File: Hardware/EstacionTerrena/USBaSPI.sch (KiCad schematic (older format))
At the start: 17 parts, among them J2 USB_B_Micro, U1 TPD2E2U06, U2 MIC5323-3.3YD5_TR, U3 MCP2210, Y1 12MHz

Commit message: Corrección de librerías en PCB de estación terrena
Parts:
- removed U2: MIC5323-3.3YD5_TR, SamacSys_Parts:SOT95P280X100-5N, symbol EstacionTerrena-rescue:MIC5323-3.3YD5_TR-SamacSys_Parts
- removed U3: MCP2210, Package_SO:SSOP-20_5.3x7.2mm_P0.65mm, symbol EstacionTerrena-rescue:MCP2210-AXTEC_IC
- added U2: MIC5323-3.3YD5_TR, SOT95P280X100-5N, symbol SamacSys_Parts:MIC5323-3.3YD5_TR
- added U3: MCP2210, symbol AXTEC_IC:MCP2210
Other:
- moved on the sheet: C4
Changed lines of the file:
@@
 EESchema Schematic File Version 4
 LIBS:EstacionTerrena-cache
-EELAYER 26 0
+EELAYER 29 0
 EELAYER END
 $Descr A4 11693 8268
@@
 Wire Wire Line
 	1100 4600 1150 4600
-$Comp
-L EstacionTerrena-rescue:MCP2210-AXTEC_IC U3
-U 1 1 5B9999E2
-P 8250 4450
-F 0 "U3" H 8250 5115 50  0000 C CNN
-F 1 "MCP2210" H 8250 5024 50  0000 C CNN
-F 2 "Package_SO:SSOP-20_5.3x7.2mm_P0.65mm" H 8050 4550 50  0001 C CNN
-F 3 "http://ww1.microchip.com/downloads/en/devicedoc/22288a.pdf" H 8050 4550 50  0001 C CNN
-F 4 "MCP2210-I/SS" H 8250 4450 50  0001 C CNN "Manufacturer Part Number"
-	1    8250 4450
-	1    0    0    -1
-$EndComp
 Text Label 1650 4150 0    50   ~ 0
 D+
@@
 L power:GND #PWR018
 U 1 1 5B9A09D3
-P 8300 3500
-F 0 "#PWR018" H 8300 3250 50  0001 C CNN
-F 1 "GND" H 8305 3327 50  0000 C CNN
-F 2 "" H 8300 3500 50  0001 C CNN
-F 3 "" H 8300 3500 50  0001 C CNN
-	1    8300 3500
+P 8250 3450
+F 0 "#PWR018" H 8250 3200 50  0001 C CNN
+F 1 "GND" H 8255 3277 50  0000 C CNN
+F 2 "" H 8250 3450 50  0001 C CNN
+F 3 "" H 8250 3450 50  0001 C CNN
+	1    8250 3450
 	1    0    0    -1
 $EndComp
@@
 L power:+3V3 #PWR017
 U 1 1 5B9A0A7A
-P 8300 3200
-F 0 "#PWR017" H 8300 3050 50  0001 C CNN
-F 1 "+3V3" H 8315 3373 50  0000 C CNN
-F 2 "" H 8300 3200 50  0001 C CNN
-F 3 "" H 8300 3200 50  0001 C CNN
-	1    8300 3200
-	1    0    0    -1
-$EndComp
-Wire Wire Line
-	8300 3250 8300 3200
-Wire Wire Line
-	8300 3450 8300 3500
+P 8250 3150
+F 0 "#PWR017" H 8250 3000 50  0001 C CNN
+F 1 "+3V3" H 8265 3323 50  0000 C CNN
+F 2 "" H 8250 3150 50  0001 C CNN
+F 3 "" H 8250 3150 50  0001 C CNN
+	1    8250 3150
+	1    0    0    -1
+$EndComp
+Wire Wire Line
+	8250 3200 8250 3150
+Wire Wire Line
+	8250 3400 8250 3450
 Wire Wire Line
 	5650 4350 5650 4300
@@
 Wire Wire Line
 	4950 3950 5650 3950
-$Comp
-L EstacionTerrena-rescue:MIC5323-3.3YD5_TR-SamacSys_Parts U2
-U 1 1 5BEF597E
-P 4550 4000
-F 0 "U2" H 4550 4317 50  0000 C CNN
-F 1 "MIC5323-3.3YD5_TR" H 4550 4225 50  0000 C CNN
-F 2 "SamacSys_Parts:SOT95P280X100-5N" H 5500 4100 50  0001 L CNN
-F 3 "http://ww1.microchip.com/downloads/en/DeviceDoc/MIC5323.pdf" H 5500 4000 50  0001 L CNN
-F 4 "Micrel MIC5323-3.3YD5 TR, LDO Voltage Regulator, 300mA, 3.3 V 2%, 2.65  5.5 Vin, 5-Pin TSOT-23" H 5500 3900 50  0001 L CNN "Description"
-F 5 "1" H 5500 3800 50  0001 L CNN "Height"
-F 6 "Micrel" H 5500 3700 50  0001 L CNN "Manufacturer_Name"
-F 7 "MIC5323-3.3YD5 TR" H 5500 3600 50  0001 L CNN "Manufacturer Part Number"
-F 8 "8855996P" H 5500 3500 50  0001 L CNN "RS Part Number"
-F 9 "http://uk.rs-online.com/web/p/products/8855996P" H 5500 3400 50  0001 L CNN "RS Price/Stock"
-F 10 "MIC5323-3.3YD5 TR" H 5500 3300 50  0001 L CNN "Arrow Part Number"
-F 11 "http://uk.rs-online.com/web/p/products/8855996P" H 5500 3200 50  0001 L CNN "Arrow Price/Stock"
-	1    4550 4000
-	1    0    0    -1
-$EndComp
 $Comp
 L Device:R R2
@@
 L Device:C_Small C4
 U 1 1 5BEF7387
-P 8300 3350
-F 0 "C4" H 8392 3396 50  0000 L CNN
-F 1 "100nF" H 8392 3305 50  0000 L CNN
-F 2 "Capacitor_SMD:C_0603_1608Metric" H 8300 3350 50  0001 C CNN
-F 3 "~" H 8300 3350 50  0001 C CNN
-F 4 "X7R" H 8300 3350 50  0001 C CNN "Dielectric"
-F 5 "16V" H 8300 3350 50  0001 C CNN "Voltage"
-F 6 "EMK107B7104KAHT" H 8300 3350 50  0001 C CNN "Manufacturer Part Number"
-	1    8300 3350
+P 8250 3300
+F 0 "C4" H 8342 3346 50  0000 L CNN
+F 1 "100nF" H 8342 3255 50  0000 L CNN
+F 2 "Capacitor_SMD:C_0603_1608Metric" H 8250 3300 50  0001 C CNN
+F 3 "~" H 8250 3300 50  0001 C CNN
+F 4 "X7R" H 8250 3300 50  0001 C CNN "Dielectric"
+F 5 "16V" H 8250 3300 50  0001 C CNN "Voltage"
+F 6 "EMK107B7104KAHT" H 8250 3300 50  0001 C CNN "Manufacturer Part Number"
+	1    8250 3300
 	1    0    0    -1
 $EndComp
@@
 EndData
 $EndBitmap
+$Comp
+L SamacSys_Parts:MIC5323-3.3YD5_TR U2
+U 1 1 5CCFA0D3
+P 4550 4000
+F 0 "U2" H 4550 4315 50  0000 C CNN
+F 1 "MIC5323-3.3YD5_TR" H 4550 4224 50  0000 C CNN
+F 2 "SOT95P280X100-5N" H 5500 4100 50  0001 L CNN
+F 3 "http://ww1.microchip.com/downloads/en/DeviceDoc/MIC5323.pdf" H 5500 4000 50  0001 L CNN
+F 4 "Micrel MIC5323-3.3YD5 TR, LDO Voltage Regulator, 300mA, 3.3 V 2%, 2.65  5.5 Vin, 5-Pin TSOT-23" H 5500 3900 50  0001 L CNN "Description"
+F 5 "1" H 5500 3800 50  0001 L CNN "Height"
+F 6 "Micrel" H 5500 3700 50  0001 L CNN "Manufacturer_Name"
+F 7 "MIC5323-3.3YD5 TR" H 5500 3600 50  0001 L CNN "Manufacturer Part Number"
+F 8 "8855996P" H 5500 3500 50  0001 L CNN "RS Part Number"
+F 9 "http://uk.rs-online.com/web/p/products/8855996P" H 5500 3400 50  0001 L CNN "RS Price/Stock"
+F 10 "MIC5323-3.3YD5 TR" H 5500 3300 50  0001 L CNN "Arrow Part Number"
+F 11 "http://uk.rs-online.com/web/p/products/8855996P" H 5500 3200 50  0001 L CNN "Arrow Price/Stock"
+	1    4550 4000
+	1    0    0    -1
+$EndComp
+$Comp
+L AXTEC_IC:MCP2210 U3
+U 1 1 5CCFD092
+P 8250 4450
+F 0 "U3" H 8250 5115 50  0000 C CNN
+F 1 "MCP2210" H 8250 5024 50  0000 C CNN
+F 2 "" H 8050 4550 50  0001 C CNN
+F 3 "http://ww1.microchip.com/downloads/en/DeviceDoc/22288A.pdf" H 8050 4550 50  0001 C CNN
+F 4 "MCP2210-I/SS" H 8250 4450 50  0001 C CNN "Manufacturer Part Number"
+	1    8250 4450
+	1    0    0    -1
+$EndComp
 $EndSCHEMATC

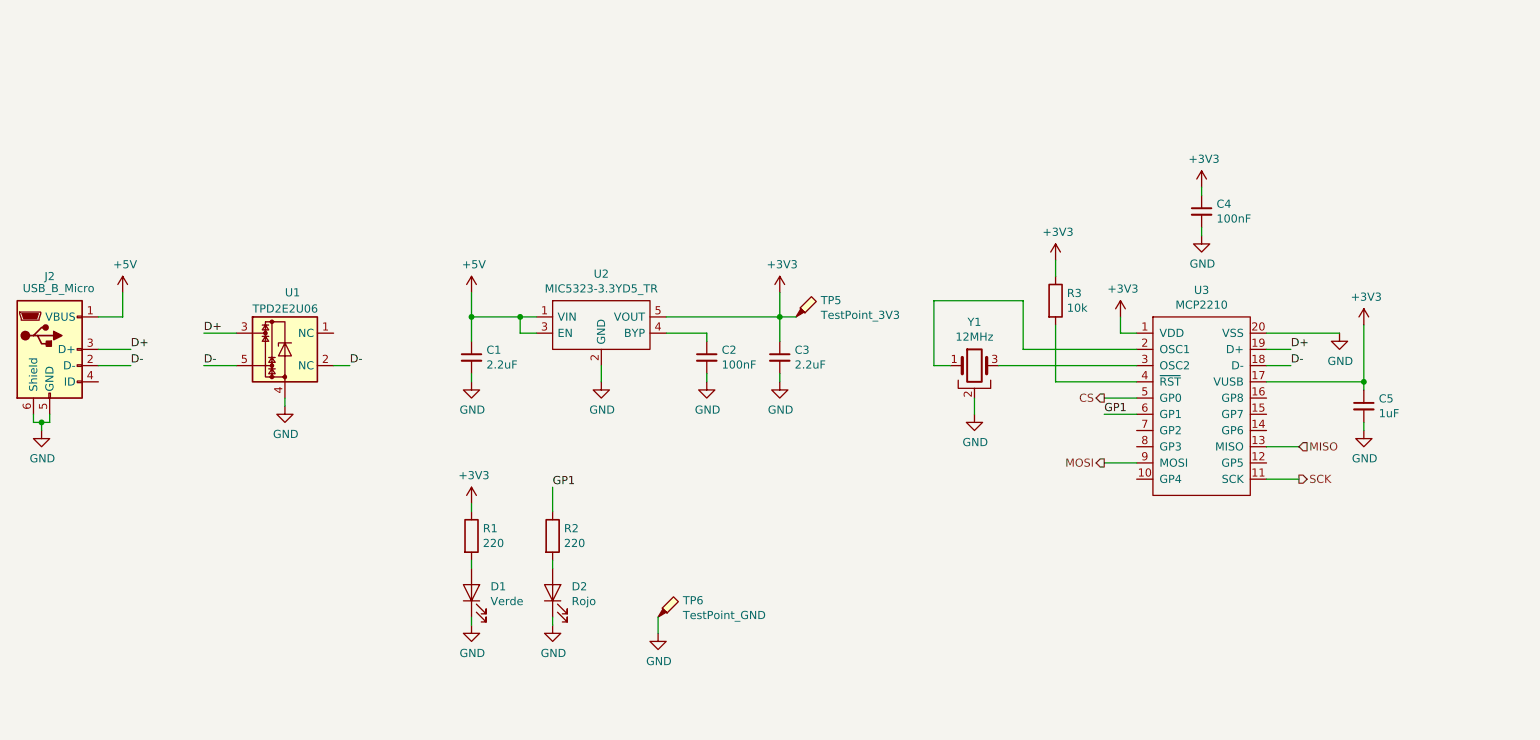
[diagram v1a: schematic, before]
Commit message: Estacion terrena:
- Nuevo LDO de 500mA para poder utilizar el CC1190 a toda su potencia de ser necesario
- Cambiado el MCP2210 por un PIC18F14K50 ya que el MCP2210 es MUY lento para transferencias SPI
- Agregado de footprints faltantes
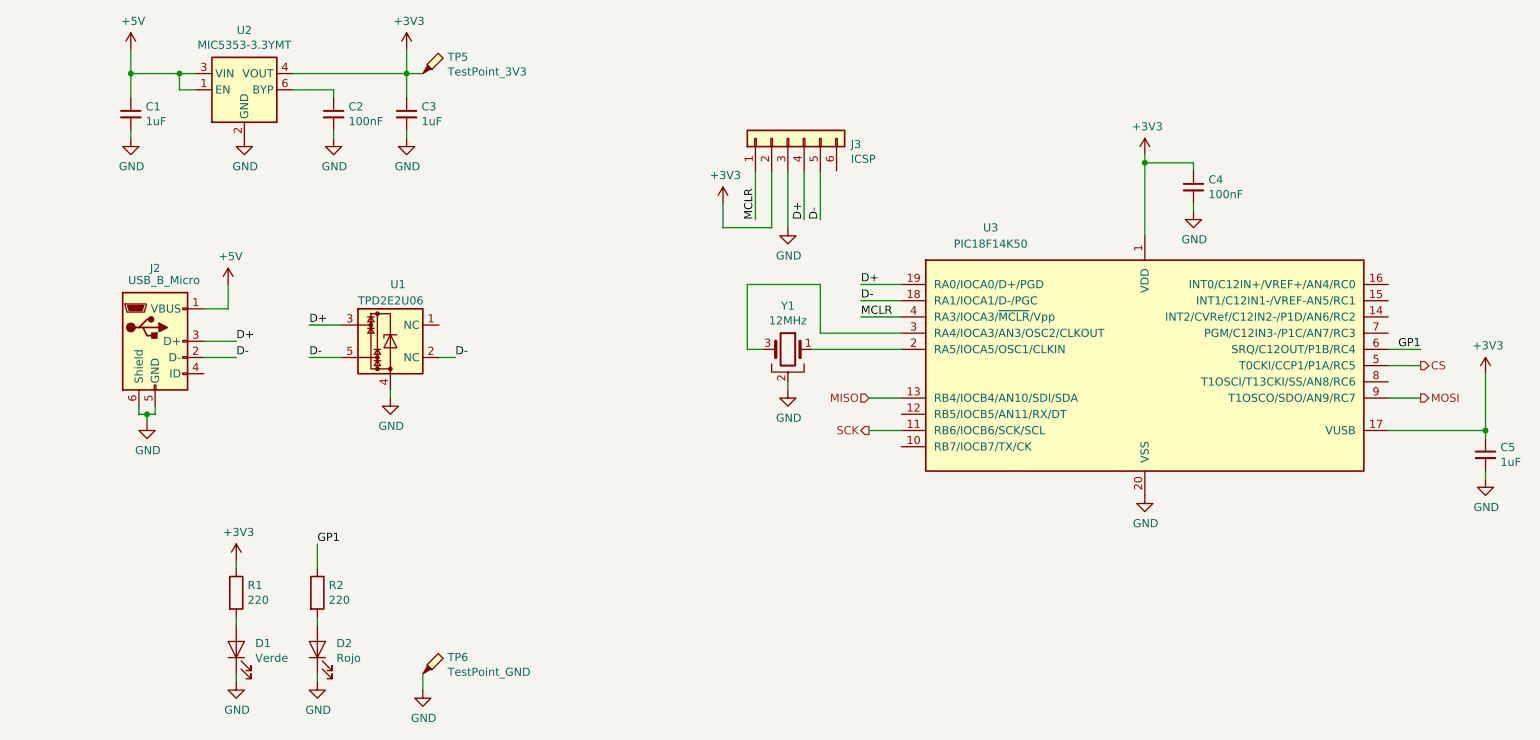
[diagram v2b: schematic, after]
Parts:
- removed R3: 10k, Resistor_SMD:R_0603_1608Metric_Pad1.05x0.95mm_HandSolder, symbol Device:R
- removed U2: MIC5323-3.3YD5_TR, SOT95P280X100-5N, symbol SamacSys_Parts:MIC5323-3.3YD5_TR
- removed U3: MCP2210, symbol AXTEC_IC:MCP2210
- added J3: ICSP, Connector_PinHeader_2.54mm:PinHeader_1x06_P2.54mm_Vertical, symbol Connector_Generic:Conn_01x06
- added U2: MIC5353-3.3YMT, Package_DFN_QFN:MLF-6-1EP_1.6x1.6mm_P0.5mm_EP0.5x1.26mm, symbol Regulator_Linear:MIC5353-3.3YMT
- added U3: PIC18F14K50, Package_SO:SSOP-20_5.3x7.2mm_P0.65mm, symbol MCU_Microchip_PIC18:PIC18F14K50-ESS
- C1, C3: value 2.2uF -> 1uF; footprint Capacitor_SMD:C_0805_2012Metric -> Capacitor_SMD:C_0603_1608Metric; Manufacturer Part Number LMK212B7225KG-T -> LMK107B7105MA-T
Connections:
- net +3V3: now also J3.2 (Pin_2), U2.4 (VOUT), U3.1 (VDD), U3.17 (VUSB)
- net +5V: now also U2.1 (EN), U2.3 (VIN)
- net CS: now also U3.5 (T0CKI/CCP1/P1A/RC5)
- net D+: now also J3.4 (Pin_4), U3.19 (RA0/IOCA0/D+/PGD)
- net D-: now also J3.5 (Pin_5), U3.18 (RA1/IOCA1/D-/PGC)
- net GND: now also J3.3 (Pin_3), U2.2 (GND), U2.7 (GND), U3.20 (VSS)
- net GP1: now also U3.6 (SRQ/C12OUT/P1B/RC4)
- net MISO: now also U3.13 (RB4/IOCB4/AN10/SDI/SDA)
- net MOSI: now also U3.9 (T1OSCO/SDO/AN9/RC7)
- net SCK: now also U3.11 (RB6/IOCB6/SCK/SCL)
- net at Y1.1: now also U3.2 (RA5/IOCA5/OSC1/CLKIN)
- net at Y1.3: now also U3.3 (RA4/IOCA3/AN3/OSC2/CLKOUT)
- net at C2.1: now also U2.6 (BYP)
- new net MCLR: J3.1 (Pin_1), U3.4 (RA3/IOCA3/~MCLR~/Vpp)
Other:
- moved on the sheet: C2, C4, D1, D2, J2, R1, R2, TP5, TP6, U1, Y1

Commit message: Nuevo conector USB para ET
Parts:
- J2: footprint Connector_USB:USB_Micro-B_Molex-105017-0001 -> Connector_USB:USB_Micro-B_Molex_47346-0001; Manufacturer Part Number 105017-0001 -> 47346-1001
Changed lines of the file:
@@
 F 0 "J2" H 1800 4550 50  0000 C CNN
 F 1 "USB_B_Micro" H 1855 4476 50  0000 C CNN
-F 2 "Connector_USB:USB_Micro-B_Molex-105017-0001" H 1950 4050 50  0001 C CNN
+F 2 "Connector_USB:USB_Micro-B_Molex_47346-0001" H 1950 4050 50  0001 C CNN
 F 3 "https://www.molex.com/webdocs/datasheets/pdf/en-us/1050170001_IO_CONNECTORS.pdf" H 1950 4050 50  0001 C CNN
-F 4 "105017-0001" H 1800 4100 50  0001 C CNN "Manufacturer Part Number"
+F 4 "47346-1001" H 1800 4100 50  0001 C CNN "Manufacturer Part Number"
 	1    1800 4100
 	1    0    0    -1
